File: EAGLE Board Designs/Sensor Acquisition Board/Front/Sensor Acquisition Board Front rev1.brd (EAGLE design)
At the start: 149.9 x 50.8 mm, 45 parts, among them J1 CONNECTOR-SENSOR_NF_S_RA_BLACK, J10 JUMPER_1X02_, J2 CONNECTOR-SENSOR_NF_S_RA_BLACK, J3 CONNECTOR-SENSOR_NF_S_RA_BLACK, J4 CONNECTOR-SENSOR_NF_S_RA_BLACK, J5 CONNECTOR-SENSOR_NF_S_RA_BLACK, J6 CONNECTOR-SENSOR_NF_S_RA_BLACK, J7 CONNECTOR-SENSOR_NF_S_RA_BLACK, J8 CONNECTOR-SENSOR_NF_S_RA_BLACK, J9 CONNECTOR-CAN_NF_S_RA_BLACK, U1 VOLTAGE_REGULATOR_SOT223_5V, U3 TCAN1051HQV-Q1

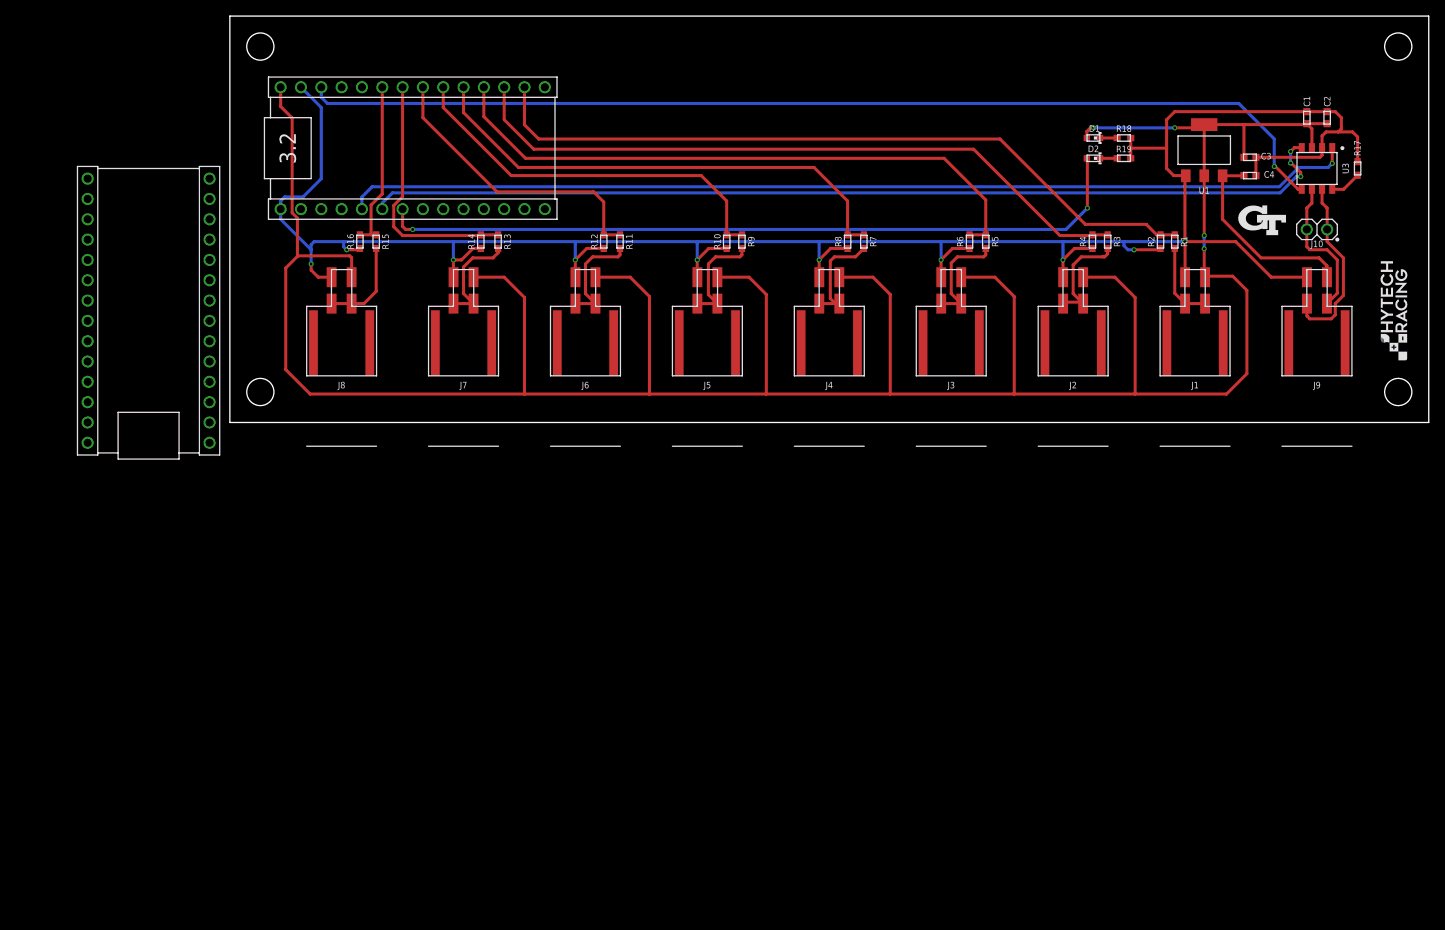
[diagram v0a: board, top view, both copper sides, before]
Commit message: Created sch for front rev 1
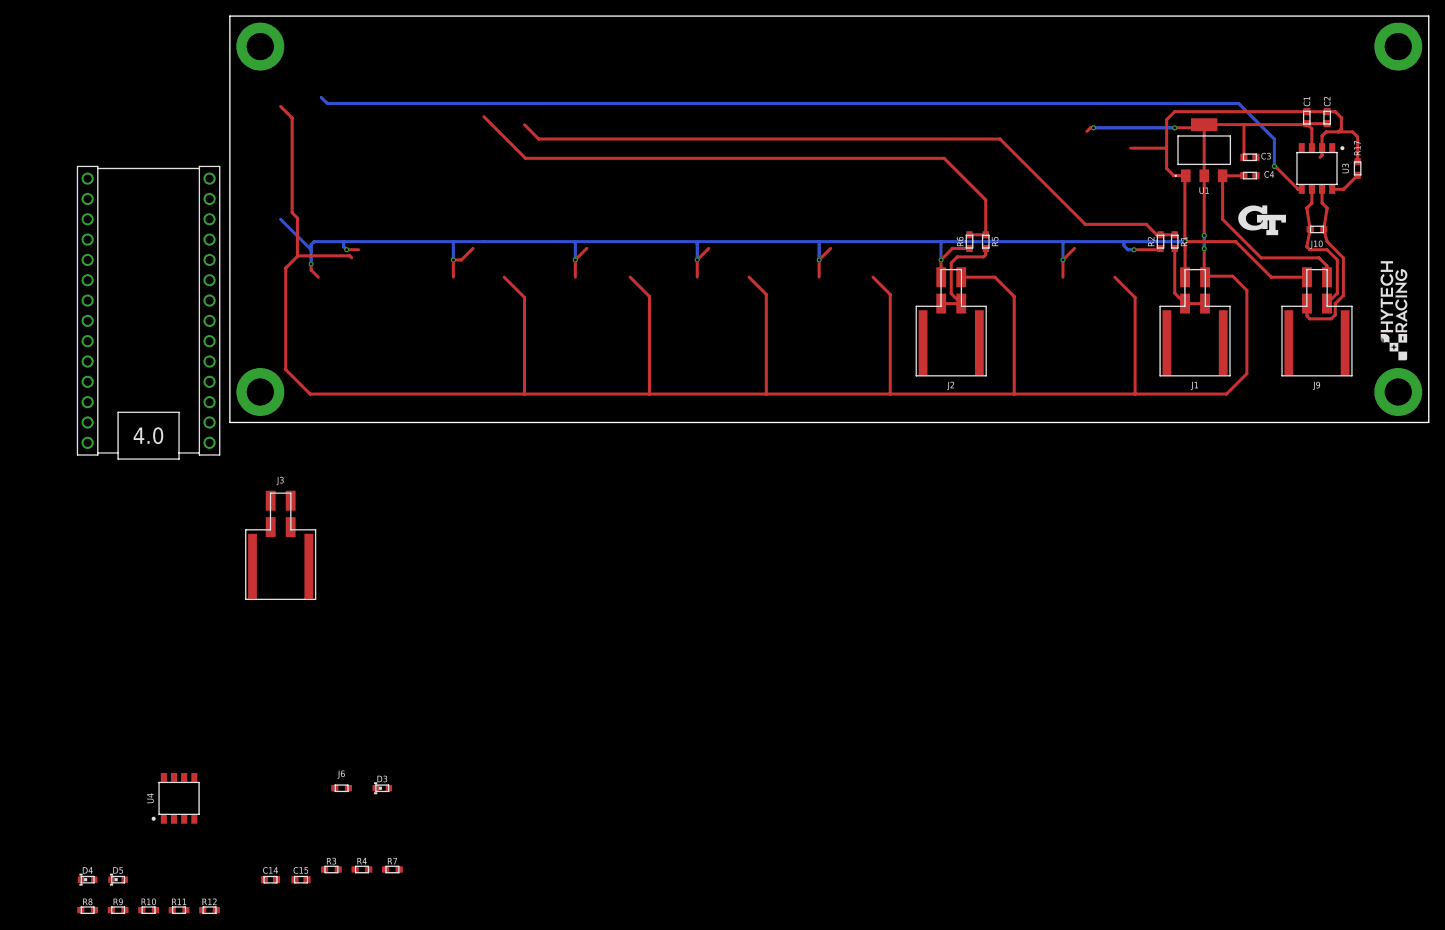
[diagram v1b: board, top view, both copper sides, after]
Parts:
- removed A1: TEENSY_3.2, HyTechDevices:TEENSY_SHORT
- removed D1, D2: LED_0603_RED, HyTechDevices:0603-LED
- removed J4, J5, J7, J8: CONNECTOR-SENSOR_NF_S_RA_BLACK, HyTechDevices:MOLEX_NANOFIT_SMD_RIGHTANGLE_04
- removed R13, R15: RESISTOR_0603_10K, HyTechDevices:0603-RES
- removed R14, R16: RESISTOR_0603_12K, HyTechDevices:0603-RES
- removed R18: RESISTOR_0603_1K, HyTechDevices:0603-RES
- removed R19: RESISTOR_0603_470, HyTechDevices:0603-RES
- added C14: CAPACITOR_0603_10V_1UF, HyTechDevices:0603-CAP
- added C15: CAPACITOR_0603_10V_0.1UF, HyTechDevices:0603-CAP
- added D3, D4, D5: LED_0603_RED, HyTechDevices:0603-LED
- added U4: TCAN1051HQV-Q1, HyTechDevices:SOIC-08(NARROW,0.15")
- J10: value JUMPER_1X02_ -> JUMPER_0603_; device HyTechDevices:1X02 -> HyTechDevices:0603-RES
- J3: value CONNECTOR-SENSOR_NF_S_RA_BLACK -> CONNECTOR-CAN_NF_S_RA_BLACK
- J6: value CONNECTOR-SENSOR_NF_S_RA_BLACK -> JUMPER_0603_; device HyTechDevices:MOLEX_NANOFIT_SMD_RIGHTANGLE_04 -> HyTechDevices:0603-RES
- R10, R4: value RESISTOR_0603_12K -> RESISTOR_0603_240
- R11, R3: value RESISTOR_0603_10K -> RESISTOR_0603_240
- R12: value RESISTOR_0603_12K -> RESISTOR_0603_10K
- R7: value RESISTOR_0603_10K -> RESISTOR_0603_1K
- R8: value RESISTOR_0603_12K -> RESISTOR_0603_470
- R9: value RESISTOR_0603_10K -> RESISTOR_0603_470
- U1: value VOLTAGE_REGULATOR_SOT223_5V -> VOLTAGE_REGULATOR_SOT-223_5V; device HyTechDevices:SOT223 -> HyTechDevices:SOT-223
- moved R8 126.5 mm to (-17.8, -61.0), turned to 0 degrees
- moved R3 124.8 mm to (12.7, -55.9), turned to 0 degrees
- moved R4 120.4 mm to (16.5, -55.9), turned to 0 degrees
- moved R9 114.3 mm to (-14.0, -61.0), turned to 0 degrees
- moved R10 110.5 mm to (-10.2, -61.0), turned to 0 degrees
- moved R11 100.1 mm to (-6.35, -61.0), turned to 0 degrees
- moved R7 98.1 mm to (20.3, -55.9), turned to 0 degrees
- moved R12 97.0 mm to (-2.54, -61.0), turned to 0 degrees
- moved J3 88.4 mm to (6.35, -11.4)
- moved J6 69.3 mm to (14.0, -45.7)
- moved J2 15.2 mm to (90.2, 16.5)
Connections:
- removed net 3.3V: A2.3.3V
- removed net AGND: A1.AGND/GND
- removed net CAN_LED: A1.D5, D2.2
- removed net CAN_RX: A1.D4, U3.4
- removed net CAN_TX: A1.D3, U3.1
- removed net N$1: D1.1, R18.1
- removed net N$10: J2.3, J2.4, R3.2
- removed net N$2: D2.1, R19.1
- removed net N$7: J6.3, J6.4, R11.2
- removed net SENSOR_3: A1.D16, R5.1, R6.2
- removed net SENSOR_4: A1.D17, R7.1, R8.2
- removed net SENSOR_5: A1.D18, R10.2, R9.1
- removed net SENSOR_6: A1.D19, R11.1, R12.2
- removed net SENSOR_7: A1.D20, R13.1, R14.2
- removed net SENSOR_8: A1.D21, R15.1, R16.2
- removed net VIN: A2.VIN
- new net CAN1_LED: A2.D5, D4.2
- new net CAN2_LED: A2.D6, D5.2
- new net CANH1: J3.4, J6.1, R10.1, R11.1, R3.1, R4.1, U4.7
- new net CANL1: J3.3, J6.2, R10.2, R11.2, R3.2, R4.2, U4.6
- new net CANRX1: A2.D23, U4.4
- new net CANRX2: A2.D0, U3.4
- new net CANTX1: A2.D22, U4.1
- new net CANTX2: A2.D1, U3.1
- net +12V: now also J3.1
- net +5V: now also A2.VIN, C14.2, C15.2, D3.2, U4.3; no longer A1.VIN, D1.2, J3.1, J4.1, J5.1, J6.1, J7.1, J8.1
- net GND: now also C14.1, C15.1, R12.2, R7.2, R8.2, R9.2, U4.2; no longer A1.GND, J4.2, J5.2, J6.2, J7.2, J8.2, R10.1, R12.1, R14.1, R16.1, R18.2, R19.2, R4.1, R8.1
- net N$11: now also J2.3, J2.4; no longer J3.3, J3.4
- net N$3: now also D3.1, R7.1; no longer J8.3, J8.4, R15.2
- net N$5: now also D4.1, R8.1; no longer J7.3, J7.4, R13.2
- net N$6: now also D5.1, R9.1; no longer J5.3, J5.4, R9.2
- net N$9: now also R12.1, U4.8; no longer J4.3, J4.4, R7.2
- net SENSOR_1: now also A2.D14; no longer A1.D14
- net SENSOR_2: now also A2.D15, R5.1, R6.2; no longer A1.D15, R3.1, R4.2
- net TEENSY_3.3V: now also A2.3.3V, U4.5; no longer A1.3.3V
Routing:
- net CAN_TX: track 126.5 -> 0.00 mm, vias 1 -> 0
- net CAN_RX: track 122.4 -> 0.00 mm, vias 3 -> 0
- net CAN_LED: track 95.3 -> 0.00 mm, vias 2 -> 0
- net SENSOR_3: track 77.1 -> 0.00 mm
- net SENSOR_4: track 62.0 -> 0.00 mm
- net SENSOR_5: track 48.9 -> 0.00 mm
- net GND: track 293.2 -> 247.6 mm
- net SENSOR_6: track 36.9 -> 0.00 mm
- net SENSOR_7: track 31.4 -> 0.00 mm
- net +5V: track 360.8 -> 334.8 mm
- net SENSOR_8: track 21.1 -> 0.00 mm
- net N$7: track 13.6 -> 0.00 mm
- net N$9: track 13.4 -> 0.00 mm
- net N$6: track 13.4 -> 0.00 mm
- net N$10: track 13.3 -> 0.00 mm
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
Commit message: Working on front board
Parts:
- removed J9: CONNECTOR-CAN_NF_S_RA_BLACK, HyTechDevices:MOLEX_NANOFIT_SMD_RIGHTANGLE_04
- removed R17: RESISTOR_0603_10K, HyTechDevices:0603-RES
- removed U4: TCAN1051HQV-Q1, HyTechDevices:SOIC-08(NARROW,0.15")
- added J4: CONNECTOR-CAN_NF_S_RA_BLACK, HyTechDevices:MOLEX_NANOFIT_SMD_RIGHTANGLE_04
- added R13: RESISTOR_0603_10K, HyTechDevices:0603-RES
- added U2: MCP2562FD, HyTechDevices:SOIC-08(NARROW,0.15")
- U3: value TCAN1051HQV-Q1 -> MCP2562FD
- moved R12 125.5 mm to (71.1, 40.6), turned to 270 degrees
- moved C14 120.0 mm to (64.8, 47.0), turned to 270 degrees
- moved C15 119.4 mm to (67.3, 47.0), turned to 270 degrees
- moved R10 119.0 mm to (66.0, 30.5)
- moved R11 114.6 mm to (66.0, 27.9)
- moved D4 111.7 mm to (44.5, 35.6)
- moved D5 111.7 mm to (48.3, 35.6)
- moved R8 111.7 mm to (44.5, 31.8)
- moved R9 111.7 mm to (48.3, 31.8)
- moved R3 105.9 mm to (66.0, 35.6)
- moved J1 104.1 mm to (16.5, 15.2)
- moved R4 101.8 mm to (66.0, 33.0)
- moved R7 99.3 mm to (48.3, 39.4)
- moved D3 88.8 mm to (44.5, 39.4)
- moved J6 85.1 mm to (66.0, 21.6)
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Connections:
- removed net N$4: R17.1, U3.8
- removed net N$9: R12.1, U4.8
- new net N$1: R12.2, U2.8
- new net N$2: R13.2, U3.8
- new net VDD: U3.3
- net +12V: now also J4.1; no longer J9.1
- net +5V: now also U2.3; no longer U3.3, U4.3
- net CANH: now also J4.4; no longer J9.4
- net CANH1: now also U2.7; no longer U4.7
- net CANL: now also J4.3; no longer J9.3
- net CANL1: now also U2.6; no longer U4.6
- net CANRX1: now also U2.4; no longer U4.4
- net CANTX1: now also U2.1; no longer U4.1
- net GND: now also J4.2, R12.1, R13.1, U2.2; no longer J9.2, R12.2, R17.2, U4.2
- net TEENSY_3.3V: now also U2.5; no longer U4.5
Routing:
- net +5V: track 334.8 -> 0.00 mm, vias 4 -> 0
- net GND: track 247.6 -> 0.00 mm, vias 10 -> 0
- net TEENSY_3.3V: track 129.3 -> 0.00 mm, vias 1 -> 0
- net SENSOR_1: track 87.0 -> 0.00 mm
- net SENSOR_2: track 73.4 -> 0.00 mm
- net +12V: track 25.0 -> 0.00 mm
- net CANH: track 22.7 -> 0.00 mm
- net CANL: track 18.0 -> 0.00 mm
- net N$11: track 13.6 -> 0.00 mm
- net N$8: track 9.93 -> 0.00 mm
- net N$4: track 3.90 -> 0.00 mm
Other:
- board size 149.9 x 50.8 mm -> 108 x 50.8 mm
- board text added: "IMU CAN-Bus"
- board text removed: "3. Steering Wheel Sensor"
- board text removed: "4. Ambient Air Humidity"
- board text removed: "5. B-L Suspension Linear Pot"
- board text removed: "6. B-R Suspension Linear Pot"
- board text removed: "7. Ambient Air Temp"
- board text removed: "8. Motor Cooling Loop Fluid Temp"

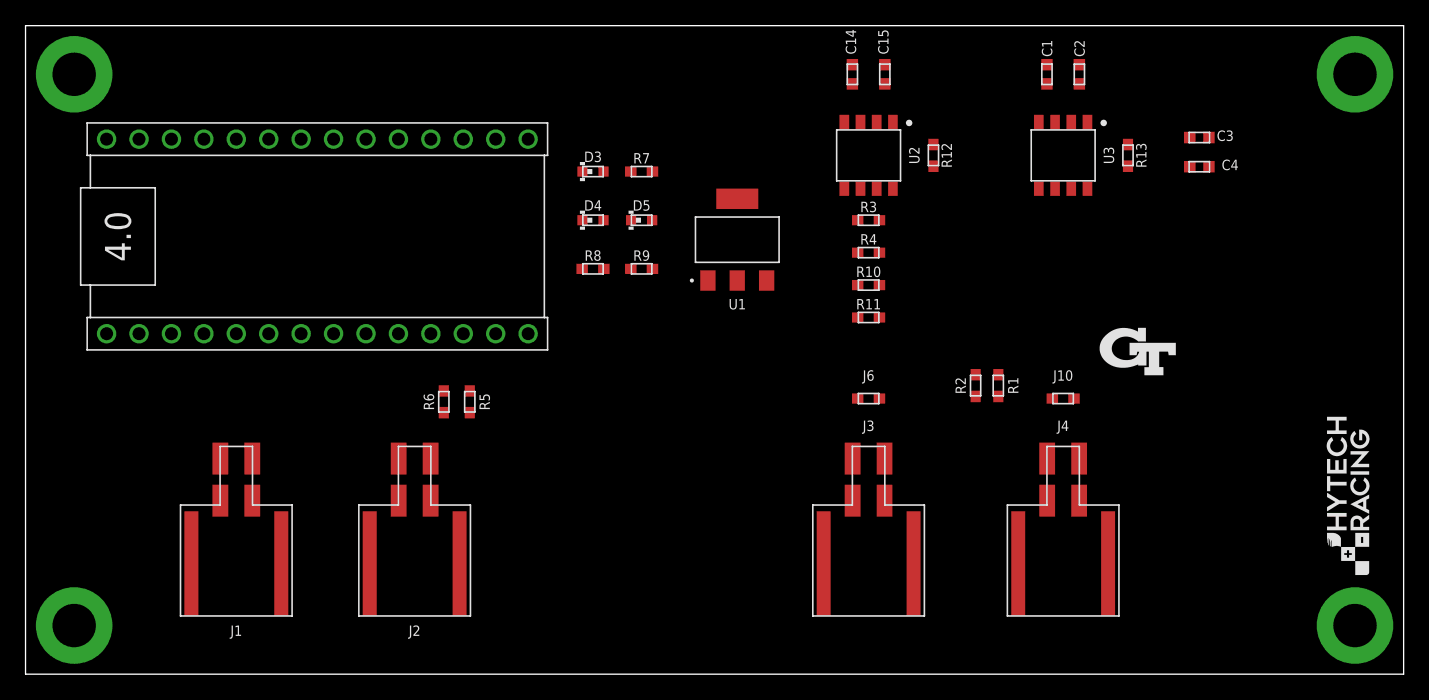
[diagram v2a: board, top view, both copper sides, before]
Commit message: Created front board
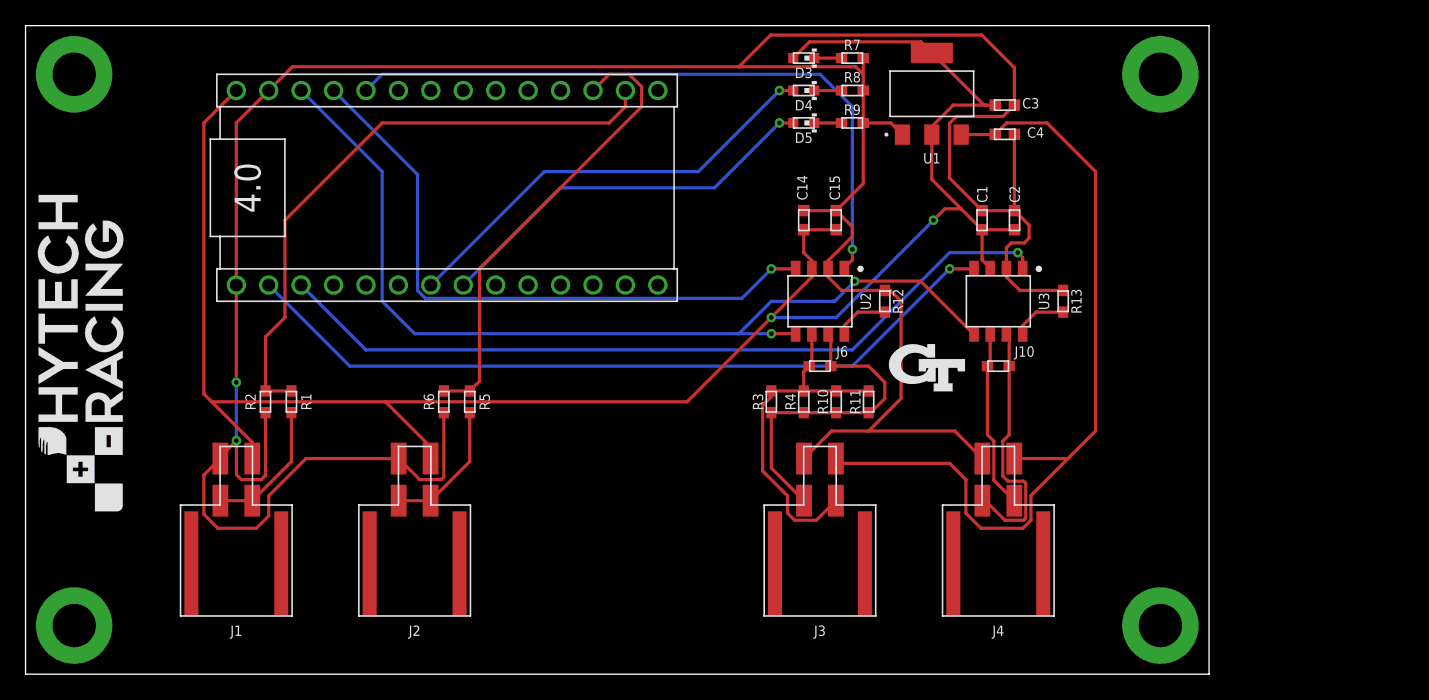
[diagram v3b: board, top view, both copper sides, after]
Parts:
- removed U$3: (no value), HyTechAesthetics:LOGO_HYTECH_0.5"
- added U$7: (no value), HyTechManufacturing:LOGO_HYTECH_MEDIUM
- moved R2 55.6 mm to (18.8, 21.3)
- moved R1 55.4 mm to (20.8, 21.3)
- moved R8 24.7 mm to (64.8, 45.7)
- moved R9 20.1 mm to (64.8, 43.2)
- moved D4 19.4 mm to (61.0, 45.7), turned to 180 degrees
- moved U1 19.0 mm to (71.0, 45.5)
- moved D3 18.8 mm to (61.0, 48.3), turned to 180 degrees
- moved R7 18.8 mm to (64.8, 48.3)
- moved U$6 16.6 mm to (70.6, 24.0)
- moved R3 16.1 mm to (58.4, 21.3), turned to 90 degrees
- moved C3 15.5 mm to (76.7, 44.6)
- moved C4 15.5 mm to (76.7, 42.3)
- moved U$1 15.2 mm to (88.9, 3.81)
- moved U$4 15.2 mm to (88.9, 47.0)
- moved D5 14.8 mm to (61.0, 43.2), turned to 180 degrees
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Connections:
- removed net VDD: U3.3
- net +5V: now also U3.3
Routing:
- net GND: track 0.00 -> 240.7 mm, vias 0 -> 2
- net +5V: track 0.00 -> 152.1 mm, vias 0 -> 2
- net TEENSY_3.3V: track 0.00 -> 74.5 mm, vias 0 -> 2
- net +12V: track 0.00 -> 65.4 mm
- net CANTX2: track 0.00 -> 62.8 mm, vias 0 -> 1
- net CANRX2: track 0.00 -> 61.1 mm, vias 0 -> 1
- net CANTX1: track 0.00 -> 52.6 mm, vias 0 -> 1
- net CANRX1: track 0.00 -> 49.2 mm, vias 0 -> 1
- net SENSOR_1: track 0.00 -> 47.7 mm
- net SENSOR_2: track 0.00 -> 36.2 mm
- net CAN1_LED: track 0.00 -> 34.7 mm, vias 0 -> 1
- net CAN2_LED: track 0.00 -> 31.1 mm, vias 0 -> 1
- net CANL1: track 0.00 -> 27.6 mm
- net CANH1: track 0.00 -> 25.9 mm
- net CANH: track 0.00 -> 20.2 mm
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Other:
- board size 108 x 50.8 mm -> 92.7 x 50.8 mm
- board text added: "IMU CAN"
- board text added: "Vehicle CAN"
- board text removed: "CAN"
